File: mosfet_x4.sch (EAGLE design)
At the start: 26 parts, among them Q1 IRLZ34N, Q2 IRLZ34N, Q3 IRLZ34N, Q4 IRLZ34N

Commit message: Updated MOSFET board
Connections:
- net +12V: now also X3-2.KL; no longer X3-1.KL
- net GND: now also X3-1.KL; no longer X3-2.KL
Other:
- moved on the sheet: X3-1, X3-2
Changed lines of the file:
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@@
 <?xml version="1.0" encoding="utf-8"?>
 <!DOCTYPE eagle SYSTEM "eagle.dtd">
-<eagle version="6.6.0">
+<eagle version="7.6.0">
 <drawing>
 <settings>
@@
 <instance part="H3" gate="G$1" x="81.28" y="104.14"/>
 <instance part="H4" gate="G$1" x="81.28" y="96.52"/>
-<instance part="X3" gate="-1" x="58.42" y="109.22"/>
-<instance part="X3" gate="-2" x="58.42" y="104.14"/>
+<instance part="X3" gate="-1" x="58.42" y="104.14"/>
+<instance part="X3" gate="-2" x="58.42" y="109.22"/>
 <instance part="P+3" gate="1" x="68.58" y="116.84"/>
 <instance part="GND5" gate="1" x="68.58" y="99.06"/>
@@
 </segment>
 <segment>
-<pinref part="X3" gate="-2" pin="KL"/>
 <wire x1="68.58" y1="101.6" x2="68.58" y2="104.14" width="0.1524" layer="91"/>
-<wire x1="68.58" y1="104.14" x2="63.5" y2="104.14" width="0.1524" layer="91"/>
 <pinref part="GND5" gate="1" pin="GND"/>
+<pinref part="X3" gate="-1" pin="KL"/>
+<wire x1="63.5" y1="104.14" x2="68.58" y2="104.14" width="0.1524" layer="91"/>
 </segment>
 <segment>
@@
 </segment>
 <segment>
-<pinref part="X3" gate="-1" pin="KL"/>
 <pinref part="P+3" gate="1" pin="+12V"/>
 <wire x1="68.58" y1="114.3" x2="68.58" y2="109.22" width="0.1524" layer="91"/>
-<wire x1="68.58" y1="109.22" x2="63.5" y2="109.22" width="0.1524" layer="91"/>
-</segment>
-<segment>
+<pinref part="X3" gate="-2" pin="KL"/>
+<wire x1="63.5" y1="109.22" x2="68.58" y2="109.22" width="0.1524" layer="91"/>
+</segment>
+<segment>

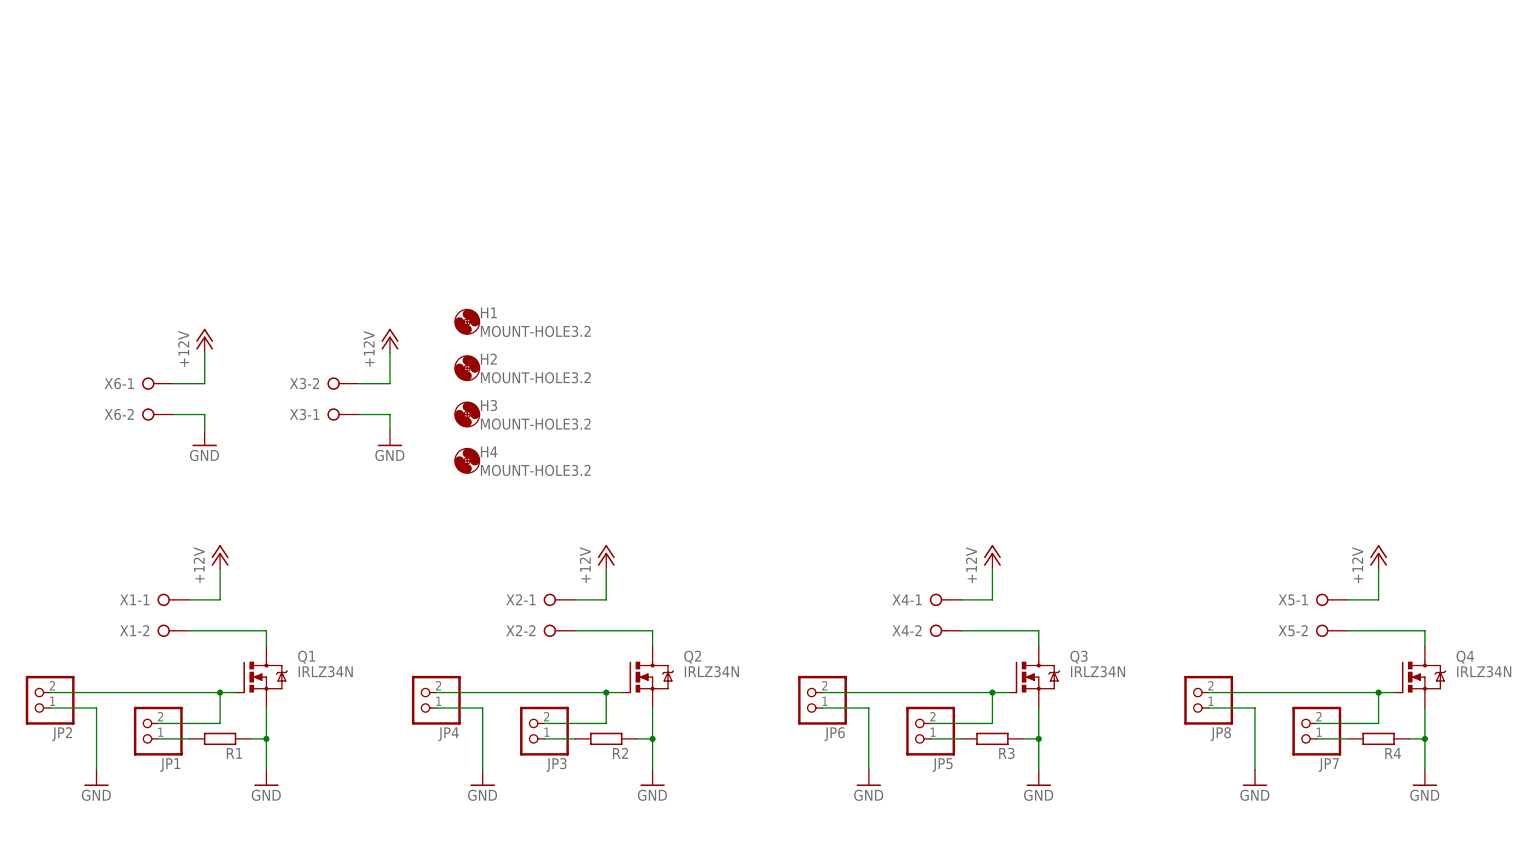
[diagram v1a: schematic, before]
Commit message: Remove pulldown enable jumpers and compact and rotate connectors.
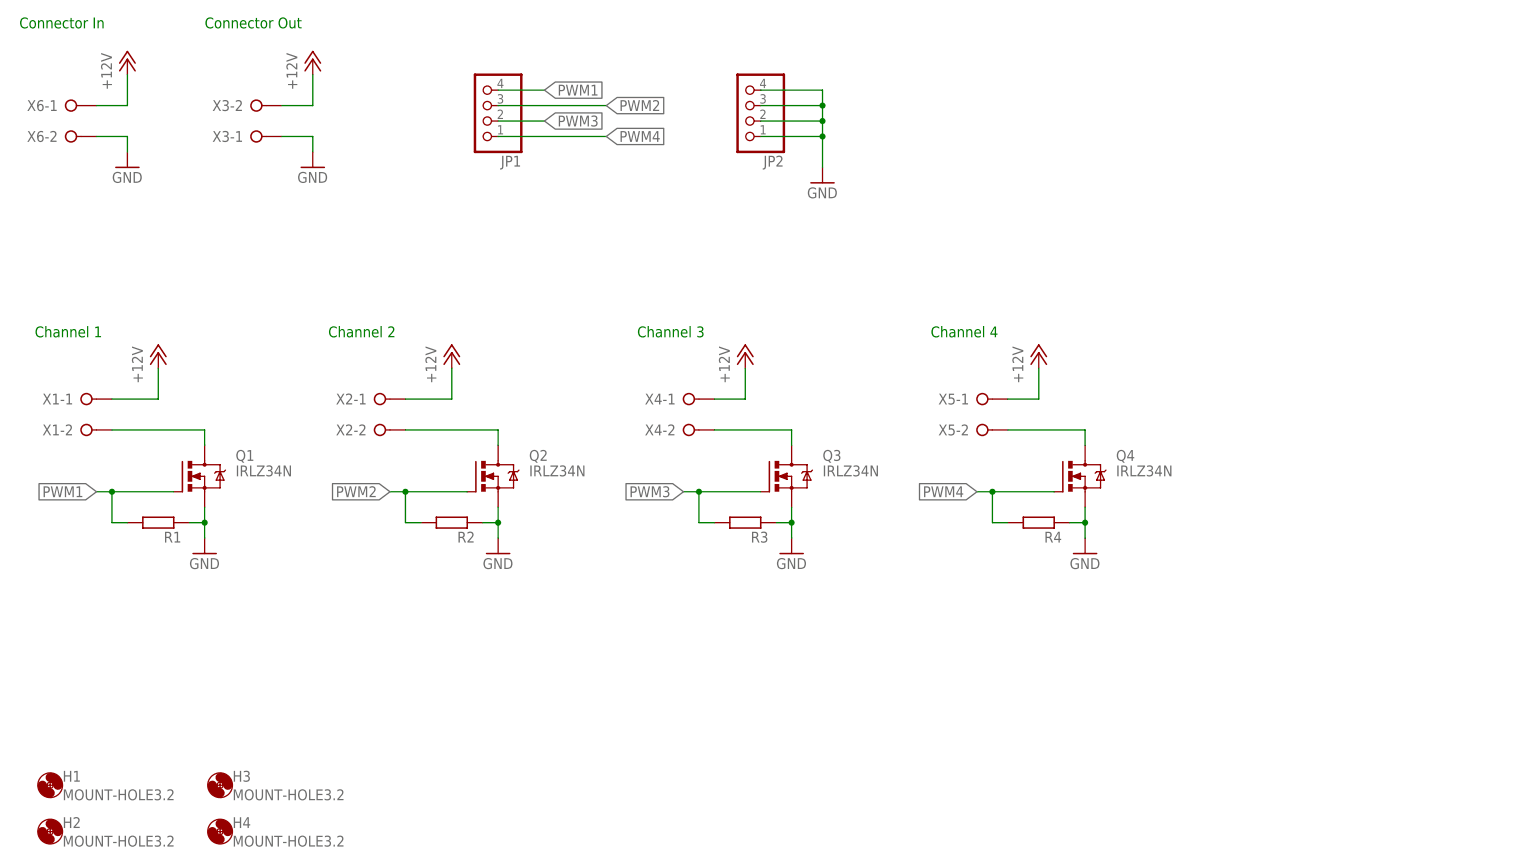
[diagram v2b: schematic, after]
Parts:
- removed JP3, JP4, JP5, JP6, JP7, JP8: (no value), pinhead:PINHD-1X2
- JP1, JP2: device pinhead:PINHD-1X2 -> pinhead:PINHD-1X4
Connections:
- removed net N$1: JP1.1, R1.2
- removed net N$10: JP7.1, R4.2
- removed net N$11: JP7.2, JP8.2, Q4.G
- removed net N$2: JP1.2, JP2.2, Q1.G
- removed net N$3: JP3.1, R2.2
- removed net N$4: JP3.2, JP4.2, Q2.G
- removed net N$7: JP5.1, R3.2
- removed net N$8: JP5.2, JP6.2, Q3.G
- new net PWM1: JP1.4, Q1.G, R1.2
- new net PWM2: JP1.3, Q2.G, R2.2
- new net PWM3: JP1.2, Q3.G, R3.2
- new net PWM4: JP1.1, Q4.G, R4.2
- net GND: now also JP2.2, JP2.3, JP2.4; no longer JP4.1, JP6.1, JP8.1
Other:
- note added: "Channel 1"
- note added: "Channel 2"
- note added: "Channel 3"
- note added: "Channel 4"
- note added: "Connector In"
- note added: "Connector Out"
- moved on the sheet: H1, H2, H3, H4, Q1, Q2, Q3, Q4, R1, R2, R3, R4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
